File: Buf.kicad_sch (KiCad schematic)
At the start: 24 parts, among them U13 74AHCT573PW, U15 74AHCT573PW, U16 74AHCT573PW, U17 74AHCT573PW, U18 74AHCT573PW, U19 74AHCT573PW, U2 74AHCT573PW, U20 74AHCT573PW, U21 74AHCT573PW, U22 74AHCT573PW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

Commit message: Toward final "A"
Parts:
- added R2 (x2): 0, stdpads:R_0603, symbol Device:R_Small
- added R2 (x2): DNP, stdpads:R_0603, symbol Device:R_Small
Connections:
- net AccA22: now also R2.1; no longer U2.3 (D1)
- net AccA23: now also R2.1; no longer U2.2 (D0)
- new net Aout22: R2.2, R2.2, U2.3 (D1)
- new net Aout23: R2.2, R2.2, U2.2 (D0)
- new net GA22: R2.1
- new net GA23: R2.1

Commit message: Update to new makefile, etc.
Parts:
- R2: value 0 -> DNP; LCSC Part C23182 -> (none)
- R2: value DNP -> 0
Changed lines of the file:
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@@
       (effects (font (size 1.27 1.27)))
     )
-    (property "Value" "0" (at 127 71.12 90)
+    (property "Value" "DNP" (at 127 71.12 90)
       (effects (font (size 1.27 1.27)) (justify bottom))
     )
@@
       (effects (font (size 1.27 1.27)) hide)
     )
-    (property "LCSC Part" "C23182" (at 127 72.39 0)
+    (property "LCSC Part" "" (at 127 72.39 0)
       (effects (font (size 1.27 1.27)) hide)
     )
@@
       (effects (font (size 1.27 1.27)))
     )
-    (property "Value" "DNP" (at 127 86.36 90)
+    (property "Value" "0" (at 127 86.36 90)
       (effects (font (size 1.27 1.27)) (justify bottom))
     )
@@
       (effects (font (size 1.27 1.27)))
     )
-    (property "Value" "0" (at 127 63.5 90)
+    (property "Value" "DNP" (at 127 63.5 90)
       (effects (font (size 1.27 1.27)) (justify bottom))
     )
@@
       (effects (font (size 1.27 1.27)) hide)
     )
-    (property "LCSC Part" "C23182" (at 127 64.77 0)
+    (property "LCSC Part" "" (at 127 64.77 0)
       (effects (font (size 1.27 1.27)) hide)
     )
@@
       (effects (font (size 1.27 1.27)))
     )
-    (property "Value" "DNP" (at 127 78.74 90)
+    (property "Value" "0" (at 127 78.74 90)
       (effects (font (size 1.27 1.27)) (justify bottom))
     )

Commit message: RC
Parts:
- renumbered R2 to R21, R2 to R22, R2 to R4, R2 to R6
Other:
- company: (none) -> Garrett's Workshop
- title: (none) -> WarpSE (GW4410A)
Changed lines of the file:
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@@
 (kicad_sch (version 20230121) (generator eeschema)
   (paper "A4")
+  (title_block
+    (title "WarpSE (GW4410A)")
+    (date "2024-03-27")
+    (rev "1.0")
+    (company "Garrett's Workshop")
+  )
   (junction (at 58.42 182.88) (diameter 0) (color 0 0 0 0)
   )
@@
   (symbol (lib_id "Device:R_Small") (at 127 72.39 270) (unit 1)
     (in_bom yes) (on_board yes) (dnp no)
-    (property "Reference" "R2" (at 127 68.58 90)
+    (property "Reference" "R6" (at 127 68.58 90)
       (effects (font (size 1.27 1.27)))
     )
@@
     (instances
       (project "WarpSE"
-        (path "/a5be2cb8-c68d-4180-8412-69a6b4c5b1d4/00000000-0000-0000-0000-000061350d21"
-          (reference "R2") (unit 1)
-        )
-        (path "/a5be2cb8-c68d-4180-8412-69a6b4c5b1d4/00000000-0000-0000-0000-000061aa52c4"
-          (reference "R20") (unit 1)
-        )
         (path "/a5be2cb8-c68d-4180-8412-69a6b4c5b1d4/00000000-0000-0000-0000-000060941922"
           (reference "R6") (unit 1)
@@
   (symbol (lib_id "Device:R_Small") (at 127 87.63 270) (unit 1)
     (in_bom yes) (on_board yes) (dnp no)
-    (property "Reference" "R2" (at 127 83.82 90)
+    (property "Reference" "R22" (at 127 83.82 90)
       (effects (font (size 1.27 1.27)))
     )
@@
     (instances
       (project "WarpSE"
-        (path "/a5be2cb8-c68d-4180-8412-69a6b4c5b1d4/00000000-0000-0000-0000-000061350d21"
-          (reference "R2") (unit 1)
-        )
-        (path "/a5be2cb8-c68d-4180-8412-69a6b4c5b1d4/00000000-0000-0000-0000-000061aa52c4"
-          (reference "R20") (unit 1)
-        )
         (path "/a5be2cb8-c68d-4180-8412-69a6b4c5b1d4/00000000-0000-0000-0000-000060941922"
           (reference "R22") (unit 1)
@@
   (symbol (lib_id "Device:R_Small") (at 127 64.77 270) (unit 1)
     (in_bom yes) (on_board yes) (dnp no)
-    (property "Reference" "R2" (at 127 60.96 90)
+    (property "Reference" "R4" (at 127 60.96 90)
       (effects (font (size 1.27 1.27)))
     )
@@
     (instances
       (project "WarpSE"
-        (path "/a5be2cb8-c68d-4180-8412-69a6b4c5b1d4/00000000-0000-0000-0000-000061350d21"
-          (reference "R2") (unit 1)
-        )
-        (path "/a5be2cb8-c68d-4180-8412-69a6b4c5b1d4/00000000-0000-0000-0000-000061aa52c4"
-          (reference "R20") (unit 1)
-        )
         (path "/a5be2cb8-c68d-4180-8412-69a6b4c5b1d4/00000000-0000-0000-0000-000060941922"
           (reference "R4") (unit 1)
@@
   (symbol (lib_id "Device:R_Small") (at 127 80.01 270) (unit 1)
     (in_bom yes) (on_board yes) (dnp no)
-    (property "Reference" "R2" (at 127 76.2 90)
+    (property "Reference" "R21" (at 127 76.2 90)
       (effects (font (size 1.27 1.27)))
     )
@@
     (instances
       (project "WarpSE"
-        (path "/a5be2cb8-c68d-4180-8412-69a6b4c5b1d4/00000000-0000-0000-0000-000061350d21"
-          (reference "R2") (unit 1)
-        )
-        (path "/a5be2cb8-c68d-4180-8412-69a6b4c5b1d4/00000000-0000-0000-0000-000061aa52c4"
-          (reference "R20") (unit 1)
-        )
         (path "/a5be2cb8-c68d-4180-8412-69a6b4c5b1d4/00000000-0000-0000-0000-000060941922"
           (reference "R21") (unit 1)

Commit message: RC
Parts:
- R21, R22: value 0 -> 47
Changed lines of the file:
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@@
   (title_block
     (title "WarpSE (GW4410A)")
-    (date "2024-03-27")
+    (date "2024-04-23")
     (rev "1.0")
     (company "Garrett's Workshop")
@@
       (effects (font (size 1.27 1.27)) hide)
     )
-    (property "Datasheet" "~" (at 58.42 185.42 0)
+    (property "Datasheet" "" (at 58.42 185.42 0)
       (effects (font (size 1.27 1.27)) hide)
     )
@@
       (effects (font (size 1.27 1.27)) hide)
     )
-    (property "Datasheet" "~" (at 68.58 185.42 0)
+    (property "Datasheet" "" (at 68.58 185.42 0)
       (effects (font (size 1.27 1.27)) hide)
     )
@@
       (effects (font (size 1.27 1.27)) hide)
     )
-    (property "Datasheet" "~" (at 78.74 185.42 0)
+    (property "Datasheet" "" (at 78.74 185.42 0)
       (effects (font (size 1.27 1.27)) hide)
     )
@@
       (effects (font (size 1.27 1.27)) hide)
     )
-    (property "Datasheet" "~" (at 48.26 185.42 0)
+    (property "Datasheet" "" (at 48.26 185.42 0)
       (effects (font (size 1.27 1.27)) hide)
     )
@@
       (effects (font (size 1.27 1.27)) hide)
     )
-    (property "Datasheet" "~" (at 99.06 185.42 0)
+    (property "Datasheet" "" (at 99.06 185.42 0)
       (effects (font (size 1.27 1.27)) hide)
     )
@@
       (effects (font (size 1.27 1.27)) hide)
     )
-    (property "Datasheet" "~" (at 88.9 185.42 0)
+    (property "Datasheet" "" (at 88.9 185.42 0)
       (effects (font (size 1.27 1.27)) hide)
     )
@@
       (effects (font (size 1.27 1.27)) hide)
     )
-    (property "Datasheet" "~" (at 58.42 175.26 0)
+    (property "Datasheet" "" (at 58.42 175.26 0)
       (effects (font (size 1.27 1.27)) hide)
     )
@@
       (effects (font (size 1.27 1.27)) hide)
     )
-    (property "Datasheet" "~" (at 68.58 175.26 0)
+    (property "Datasheet" "" (at 68.58 175.26 0)
       (effects (font (size 1.27 1.27)) hide)
     )
@@
       (effects (font (size 1.27 1.27)) hide)
     )
-    (property "Datasheet" "~" (at 78.74 175.26 0)
+    (property "Datasheet" "" (at 78.74 175.26 0)
       (effects (font (size 1.27 1.27)) hide)
     )
@@
       (effects (font (size 1.27 1.27)) hide)
     )
-    (property "Datasheet" "~" (at 48.26 175.26 0)
+    (property "Datasheet" "" (at 48.26 175.26 0)
       (effects (font (size 1.27 1.27)) hide)
     )
@@
       (effects (font (size 1.27 1.27)) hide)
     )
-    (property "Datasheet" "~" (at 99.06 175.26 0)
+    (property "Datasheet" "" (at 99.06 175.26 0)
       (effects (font (size 1.27 1.27)) hide)
     )
@@
       (effects (font (size 1.27 1.27)) hide)
     )
-    (property "Datasheet" "~" (at 88.9 175.26 0)
+    (property "Datasheet" "" (at 88.9 175.26 0)
       (effects (font (size 1.27 1.27)) hide)
     )
@@
       (effects (font (size 1.27 1.27)) hide)
     )
-    (property "Datasheet" "~" (at 127 72.39 0)
+    (property "Datasheet" "" (at 127 72.39 0)
       (effects (font (size 1.27 1.27)) hide)
     )
@@
       (effects (font (size 1.27 1.27)))
     )
-    (property "Value" "0" (at 127 86.36 90)
+    (property "Value" "47" (at 127 86.36 90)
       (effects (font (size 1.27 1.27)) (justify bottom))
     )
@@
       (effects (font (size 1.27 1.27)) hide)
     )
-    (property "Datasheet" "~" (at 127 87.63 0)
+    (property "Datasheet" "" (at 127 87.63 0)
       (effects (font (size 1.27 1.27)) hide)
     )
@@
       (effects (font (size 1.27 1.27)) hide)
     )
-    (property "Datasheet" "~" (at 127 64.77 0)
+    (property "Datasheet" "" (at 127 64.77 0)
       (effects (font (size 1.27 1.27)) hide)
     )
@@
       (effects (font (size 1.27 1.27)))
     )
-    (property "Value" "0" (at 127 78.74 90)
+    (property "Value" "47" (at 127 78.74 90)
       (effects (font (size 1.27 1.27)) (justify bottom))
     )
@@
       (effects (font (size 1.27 1.27)) hide)
     )
-    (property "Datasheet" "~" (at 127 80.01 0)
+    (property "Datasheet" "" (at 127 80.01 0)
       (effects (font (size 1.27 1.27)) hide)
     )

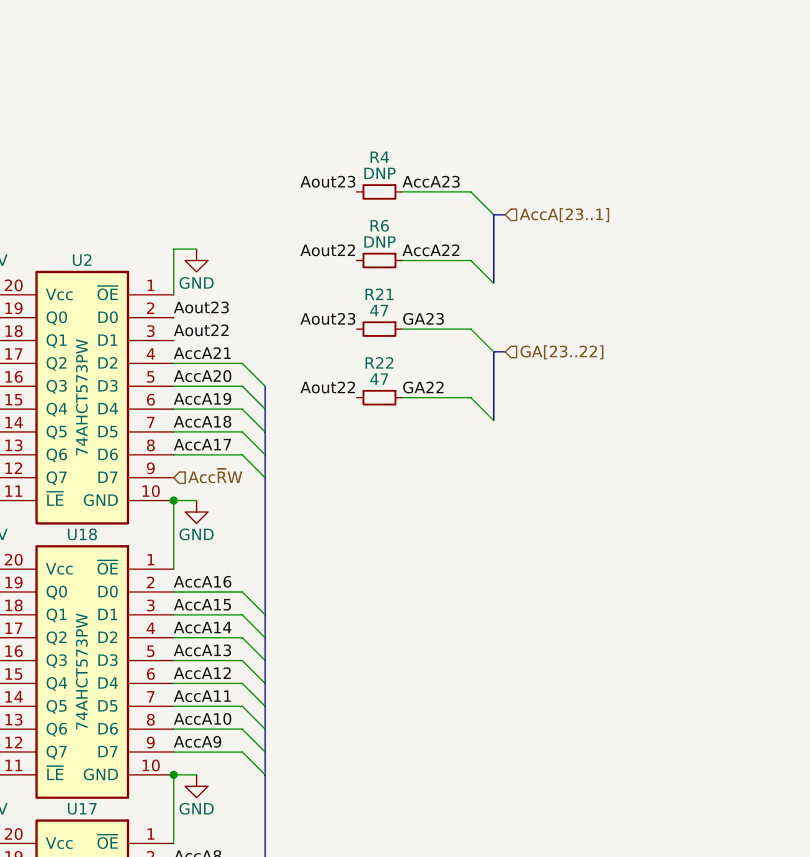
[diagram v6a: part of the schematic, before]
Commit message: Board prerelease revision 3 with USB power, A[23:20] remapping
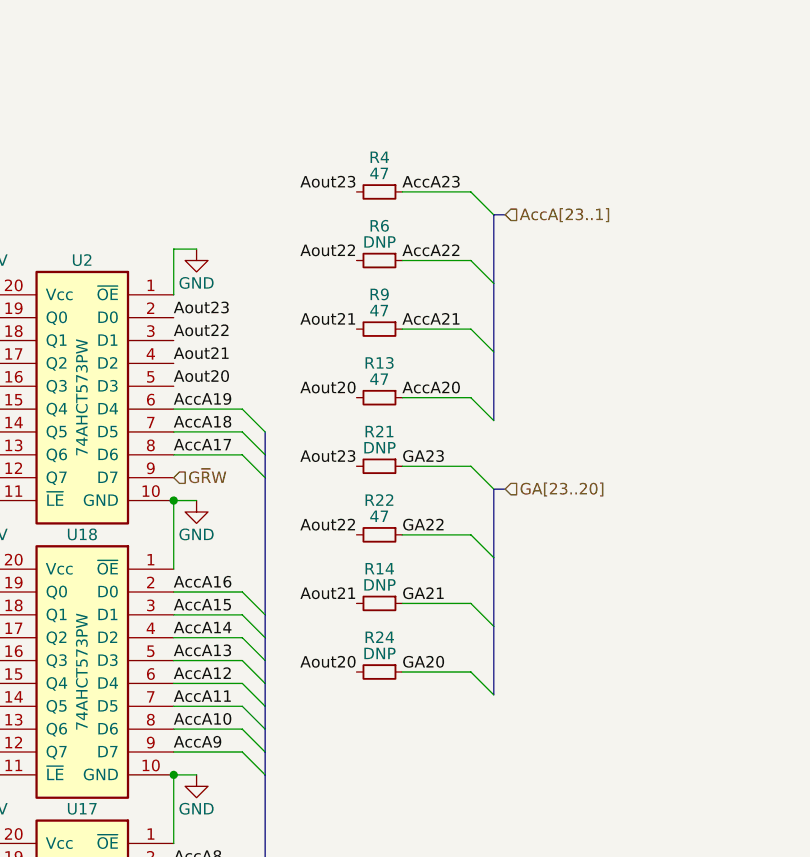
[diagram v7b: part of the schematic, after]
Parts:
- added R13, R9: 47, stdpads:R_0603, symbol Device:R_Small
- added R14, R24: DNP, stdpads:R_0603, symbol Device:R_Small
- R21: value 47 -> DNP; LCSC Part C23182 -> (none)
- R4: value DNP -> 47; LCSC Part (none) -> C23182
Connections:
- net AccA20: now also R13.1; no longer U2.5 (D3)
- net AccA21: now also R9.1; no longer U2.4 (D2)
- net Acc~{R}W renamed G~{R}W
- new net Aout20: R13.2, R24.2, U2.5 (D3)
- new net Aout21: R14.2, R9.2, U2.4 (D2)
- new net GA20: R24.1
- new net GA21: R14.1
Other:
- moved on the sheet: R22
